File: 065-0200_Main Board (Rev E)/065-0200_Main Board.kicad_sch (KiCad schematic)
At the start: 1 part

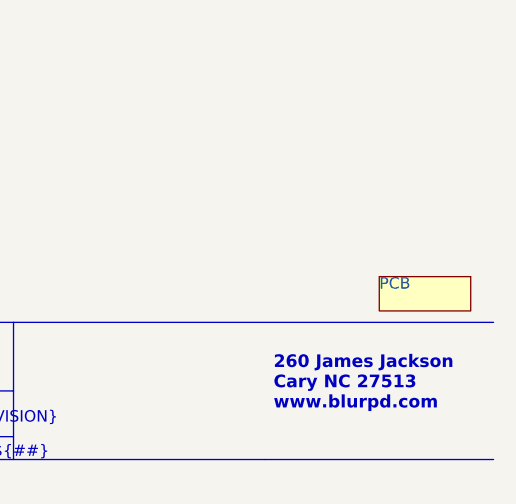
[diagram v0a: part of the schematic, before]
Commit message: Add OLED connector, annotate schematics, place all components on B.Cu
- Added J7 (GME12864-13 OLED) 4-pin I2C connector on Page 3 Micro,
  wired to SDA/SCL nets shared with the nRF module
- Auto-annotated power symbols across all schematic pages (#PWR? → numbered)
- Ran Update PCB from Schematic; all components placed on B.Cu
  ready for manual placement and routing

Co-Authored-By: Claude Sonnet 4.6 <noreply@anthropic.com>
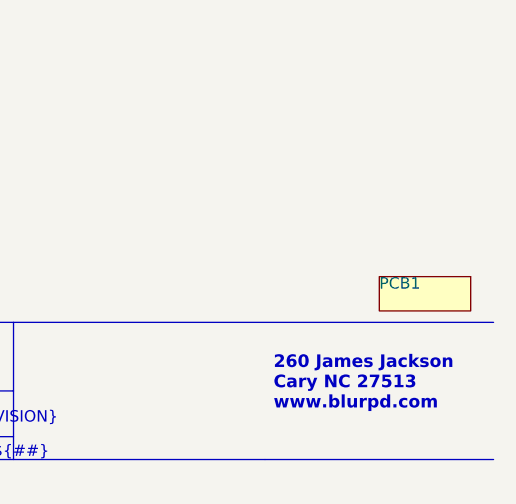
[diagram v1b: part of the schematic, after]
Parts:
- renumbered PCB to PCB1
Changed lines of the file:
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@@
 		(in_pos_files yes)
 		(dnp no)
-		(property "Reference" "PCB"
+		(property "Reference" "PCB1"
 			(at 414.02 269.0622 90)
 			(show_name no)
@@
 			(project "065-0200_Main Board"
 				(path "/2b9b3cc1-0bfe-481c-a67e-cf555aa233af"
-					(reference "PCB")
+					(reference "PCB1")
 					(unit 1)
 				)
